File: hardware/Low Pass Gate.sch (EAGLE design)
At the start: 87 parts, among them IC2 LM397, IC5 LM397, P1 POWER_SIMPLE10_SHROUDED, U1 OPAMP-QUADSO14, U2 OPAMP-QUADSO14

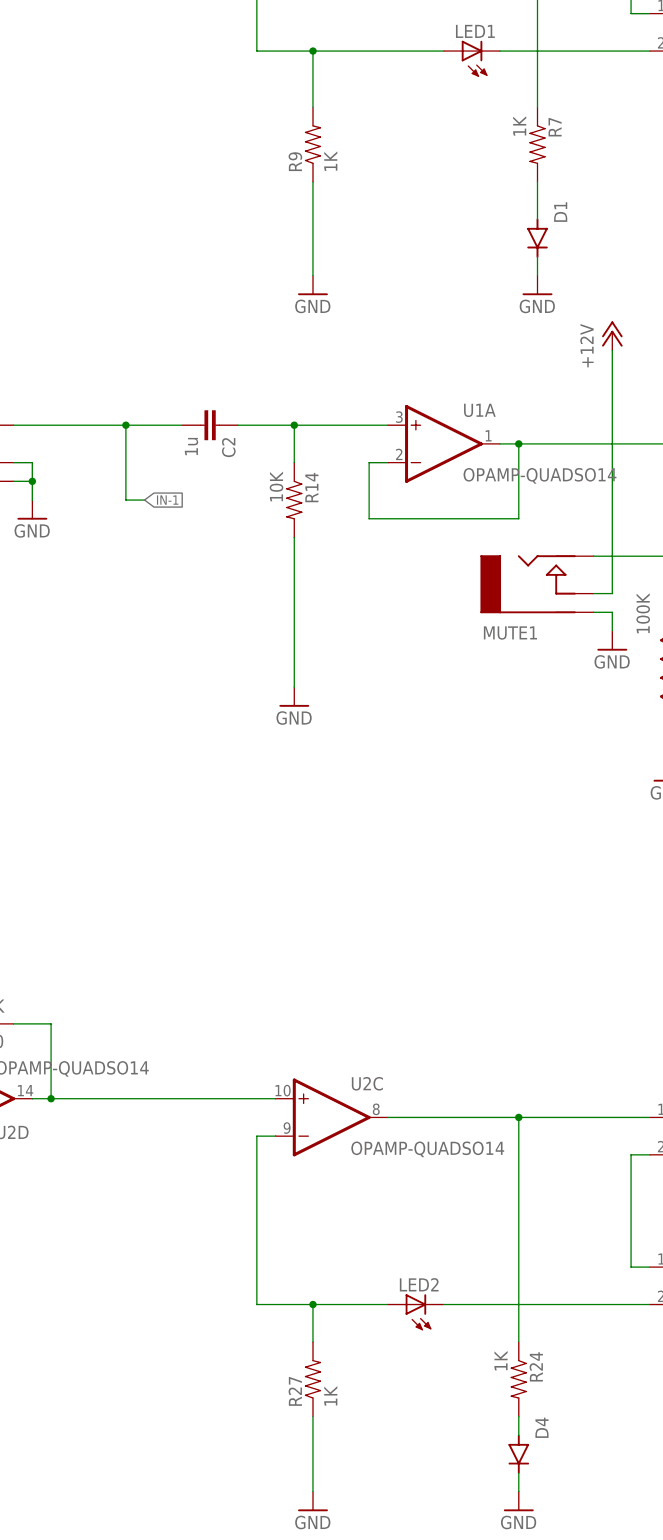
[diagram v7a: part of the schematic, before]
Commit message: adjust led drive current resistor
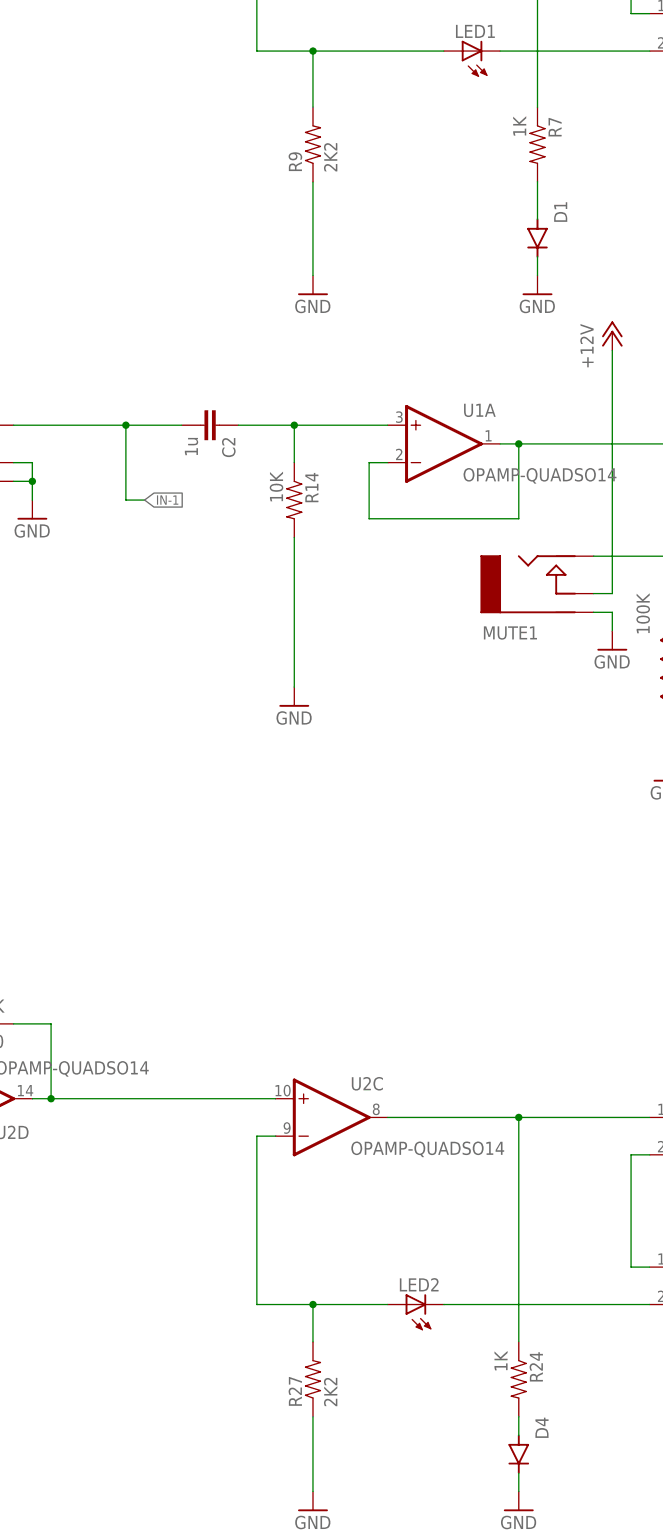
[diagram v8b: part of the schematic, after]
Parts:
- R27, R9: value 1K -> 2K2
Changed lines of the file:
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@@
 <part name="GND5" library="SparkFun-Aesthetics" library_urn="urn:adsk.eagle:library:507" deviceset="GND" device=""/>
 <part name="R7" library="SparkFun-Passives" deviceset="RESISTOR" device="0603-RES" value="1K"/>
-<part name="R9" library="SparkFun-Passives" deviceset="RESISTOR" device="0603-RES" value="1K"/>
+<part name="R9" library="SparkFun-Passives" deviceset="RESISTOR" device="0603-RES" value="2K2"/>
 <part name="GND7" library="SparkFun-Aesthetics" library_urn="urn:adsk.eagle:library:507" deviceset="GND" device=""/>
-<part name="R27" library="SparkFun-Passives" deviceset="RESISTOR" device="0603-RES" value="1K"/>
+<part name="R27" library="SparkFun-Passives" deviceset="RESISTOR" device="0603-RES" value="2K2"/>
 <part name="GND31" library="SparkFun-Aesthetics" library_urn="urn:adsk.eagle:library:507" deviceset="GND" device=""/>
 <part name="GND4" library="SparkFun-Aesthetics" library_urn="urn:adsk.eagle:library:507" deviceset="GND" device=""/>
